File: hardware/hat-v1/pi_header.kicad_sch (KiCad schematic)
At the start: 12 parts, among them J2 Pi 40-pin (female, 11 mm stac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, U10 CAT24C32WI-GT3

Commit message: HAT v1 schematic: apply adversarial review (power + digital/security/DFM)
AUTO-ON above buck EN window, BENCH no longer blocks power-off, OVP moved
to 19.2 V with input damper, Tier A parts DNP for JLC, debug links
removable for production, antenna short limited, stock footprints where
available, cap ratings/DC-bias fixes, CONSOLE_TX/RX naming.

Co-Authored-By: Claude Opus 5.5 <noreply@anthropic.com>
Claude-Session: https://claude.ai/code/session_01MLRuxTEmuMV82xcNLE62jW
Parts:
- H1, H2, H3, H4, JP4: now left out of the parts list
- U10: now not fitted
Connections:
- net UART0_RX renamed CONSOLE_RX
- net UART0_TX renamed CONSOLE_TX
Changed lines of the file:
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@@
     (property "Intersheetrefs" "${INTERSHEET_REFS}" (at 81.28 33.02 0) (effects (font (size 1.27 1.27)) hide)))
   (wire (pts (xy 78.74 35.56) (xy 81.28 35.56)) (stroke (width 0) (type default)))
-  (global_label "UART0_TX" (shape passive) (at 81.28 35.56 0) (fields_autoplaced) (effects (font (size 1.27 1.27)) (justify left))
+  (global_label "CONSOLE_TX" (shape passive) (at 81.28 35.56 0) (fields_autoplaced) (effects (font (size 1.27 1.27)) (justify left))
     (property "Intersheetrefs" "${INTERSHEET_REFS}" (at 81.28 35.56 0) (effects (font (size 1.27 1.27)) hide)))
   (wire (pts (xy 78.74 38.1) (xy 81.28 38.1)) (stroke (width 0) (type default)))
-  (global_label "UART0_RX" (shape passive) (at 81.28 38.1 0) (fields_autoplaced) (effects (font (size 1.27 1.27)) (justify left))
+  (global_label "CONSOLE_RX" (shape passive) (at 81.28 38.1 0) (fields_autoplaced) (effects (font (size 1.27 1.27)) (justify left))
     (property "Intersheetrefs" "${INTERSHEET_REFS}" (at 81.28 38.1 0) (effects (font (size 1.27 1.27)) hide)))
   (wire (pts (xy 78.74 40.64) (xy 81.28 40.64)) (stroke (width 0) (type default)))
@@
   (global_label "SPI1_SCLK" (shape passive) (at 81.28 76.2 0) (fields_autoplaced) (effects (font (size 1.27 1.27)) (justify left))
     (property "Intersheetrefs" "${INTERSHEET_REFS}" (at 81.28 76.2 0) (effects (font (size 1.27 1.27)) hide)))
-  (symbol (lib_id "batman:EEPROM_24") (at 121.92 34.29 0) (unit 1) (in_bom yes) (on_board yes) (dnp no)
+  (symbol (lib_id "batman:EEPROM_24") (at 121.92 34.29 0) (unit 1) (in_bom yes) (on_board yes) (dnp yes)
     (property "Reference" "U10" (at 115.57 24.13 0) (effects (font (size 1.27 1.27)) (justify left bottom)))
     (property "Value" "CAT24C32WI-GT3" (at 115.57 45.72 0) (effects (font (size 1.27 1.27)) (justify left top)))
@@
   (global_label "3V3_PI" (shape passive) (at 200.66 26.67 0) (fields_autoplaced) (effects (font (size 1.27 1.27)) (justify left))
     (property "Intersheetrefs" "${INTERSHEET_REFS}" (at 200.66 26.67 0) (effects (font (size 1.27 1.27)) hide)))
-  (symbol (lib_id "batman:SJ") (at 228.6 26.67 0) (unit 1) (in_bom yes) (on_board yes) (dnp no)
+  (symbol (lib_id "batman:SJ") (at 228.6 26.67 0) (unit 1) (in_bom no) (on_board yes) (dnp no)
     (property "Reference" "JP4" (at 228.6 24.13 0) (effects (font (size 1.27 1.27)) (justify bottom)))
     (property "Value" "EEP-WRITE (open)" (at 228.6 29.21 0) (effects (font (size 1.27 1.27)) (justify top)))
@@
   (global_label "3V3_PI" (shape passive) (at 115.57 90.17 0) (fields_autoplaced) (effects (font (size 1.27 1.27)) (justify left))
     (property "Intersheetrefs" "${INTERSHEET_REFS}" (at 115.57 90.17 0) (effects (font (size 1.27 1.27)) hide)))
-  (symbol (lib_id "batman:MH") (at 142.24 90.17 0) (unit 1) (in_bom yes) (on_board yes) (dnp no)
+  (symbol (lib_id "batman:MH") (at 142.24 90.17 0) (unit 1) (in_bom no) (on_board yes) (dnp no)
     (property "Reference" "H1" (at 142.24 87.63 0) (effects (font (size 1.27 1.27)) (justify bottom)))
     (property "Value" "M2.5" (at 142.24 92.71 0) (effects (font (size 1.27 1.27)) (justify top)))
@@
   (global_label "GND" (shape passive) (at 137.16 90.17 180) (fields_autoplaced) (effects (font (size 1.27 1.27)) (justify right))
     (property "Intersheetrefs" "${INTERSHEET_REFS}" (at 137.16 90.17 0) (effects (font (size 1.27 1.27)) hide)))
-  (symbol (lib_id "batman:MH") (at 162.56 90.17 0) (unit 1) (in_bom yes) (on_board yes) (dnp no)
+  (symbol (lib_id "batman:MH") (at 162.56 90.17 0) (unit 1) (in_bom no) (on_board yes) (dnp no)
     (property "Reference" "H2" (at 162.56 87.63 0) (effects (font (size 1.27 1.27)) (justify bottom)))
     (property "Value" "M2.5" (at 162.56 92.71 0) (effects (font (size 1.27 1.27)) (justify top)))
@@
   (global_label "GND" (shape passive) (at 157.48 90.17 180) (fields_autoplaced) (effects (font (size 1.27 1.27)) (justify right))
     (property "Intersheetrefs" "${INTERSHEET_REFS}" (at 157.48 90.17 0) (effects (font (size 1.27 1.27)) hide)))
-  (symbol (lib_id "batman:MH") (at 182.88 90.17 0) (unit 1) (in_bom yes) (on_board yes) (dnp no)
+  (symbol (lib_id "batman:MH") (at 182.88 90.17 0) (unit 1) (in_bom no) (on_board yes) (dnp no)
     (property "Reference" "H3" (at 182.88 87.63 0) (effects (font (size 1.27 1.27)) (justify bottom)))
     (property "Value" "M2.5" (at 182.88 92.71 0) (effects (font (size 1.27 1.27)) (justify top)))
@@
   (global_label "GND" (shape passive) (at 177.8 90.17 180) (fields_autoplaced) (effects (font (size 1.27 1.27)) (justify right))
     (property "Intersheetrefs" "${INTERSHEET_REFS}" (at 177.8 90.17 0) (effects (font (size 1.27 1.27)) hide)))
-  (symbol (lib_id "batman:MH") (at 203.2 90.17 0) (unit 1) (in_bom yes) (on_board yes) (dnp no)
+  (symbol (lib_id "batman:MH") (at 203.2 90.17 0) (unit 1) (in_bom no) (on_board yes) (dnp no)
     (property "Reference" "H4" (at 203.2 87.63 0) (effects (font (size 1.27 1.27)) (justify bottom)))
     (property "Value" "M2.5" (at 203.2 92.71 0) (effects (font (size 1.27 1.27)) (justify top)))

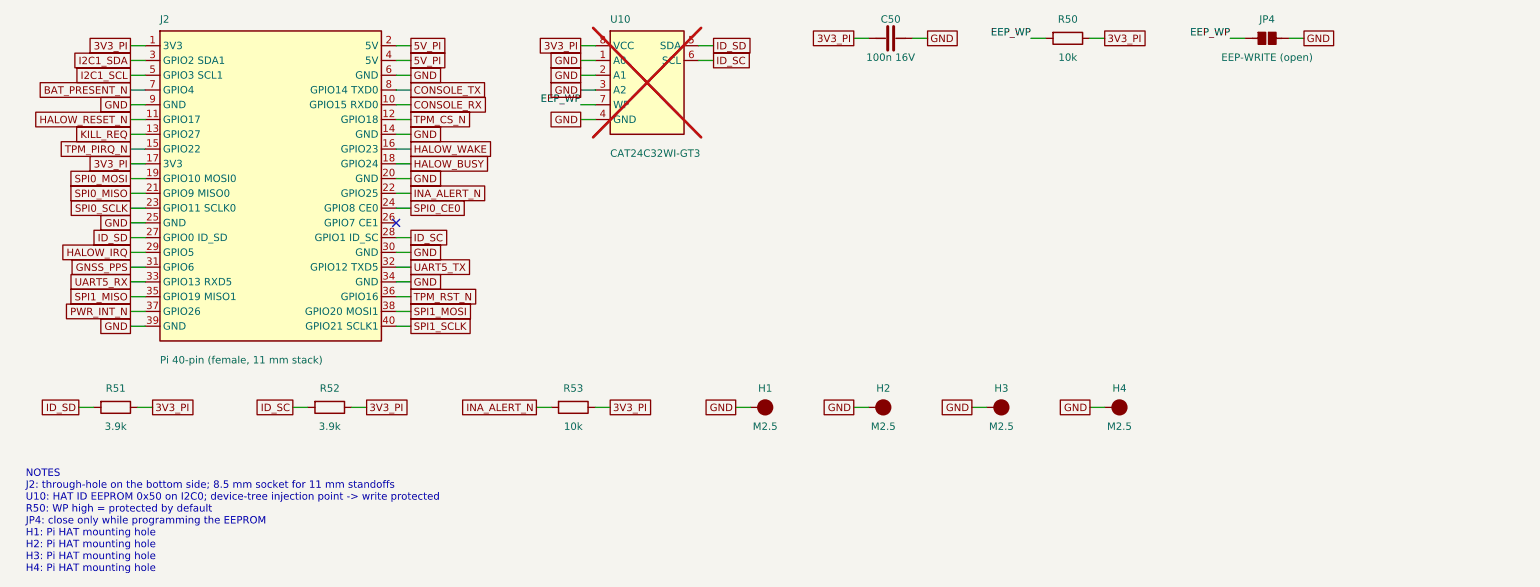
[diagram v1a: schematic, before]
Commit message: HAT v1: reduce test points (clip pads only for VBAT/5V/3V3 HaLow/GND), re-place
Signals on the 40-pin header are probed on its solder joints; checker
verifies that list. Floorplan: all functional parts and the 4 clip pads
fit; 23 small probe pads still need a home.

Co-Authored-By: Claude Opus 5.5 <noreply@anthropic.com>
Claude-Session: https://claude.ai/code/session_01MLRuxTEmuMV82xcNLE62jW
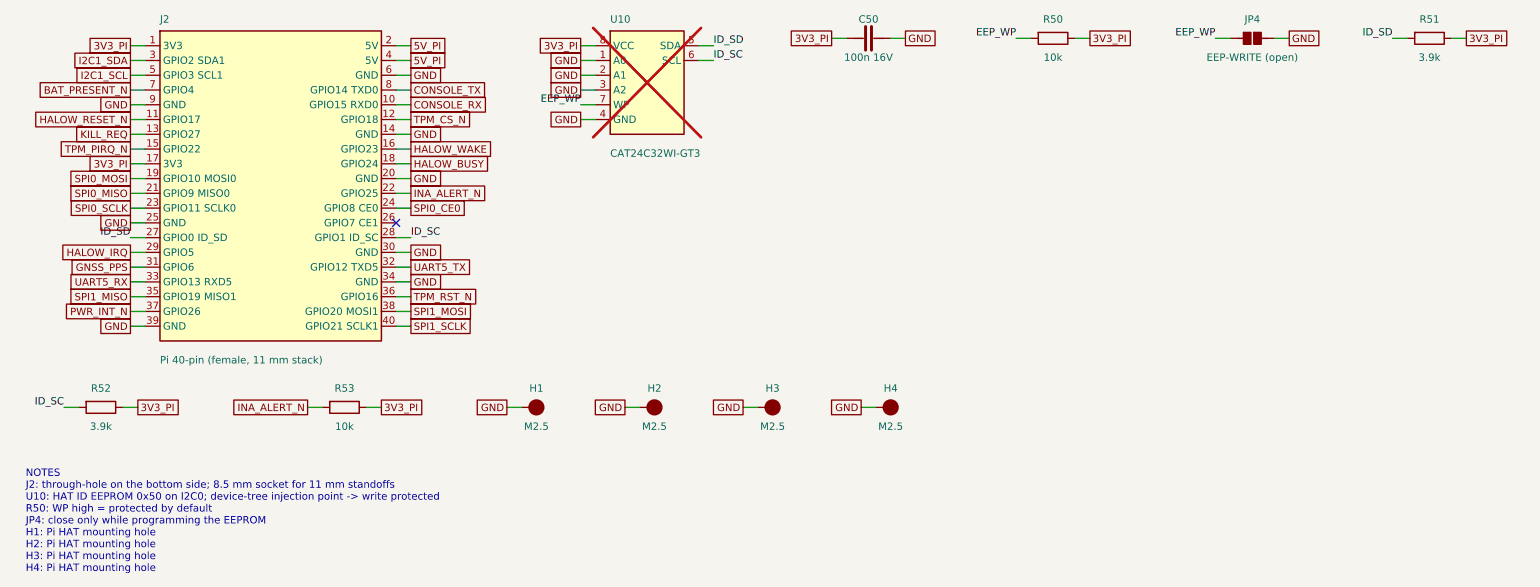
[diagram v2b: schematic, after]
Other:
- moved on the sheet: C50, H1, H2, H3, H4, JP4, R50, R51, R52, R53

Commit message: HAT v1: option D power tree - HaLow 3.3 V buck fed from the Pi 5 V rail
- TPS62933F input moved from the OR node to 5V_PI (HAT 5 V buck or Pi USB-C),
  as on the WM1302 HAT: the HaLow card still runs on USB-C only
- EN pulled up to the Pi 3.3 V through 100k: no back-feed into an unpowered Pi,
  HAT+ STANDBY turns the card off; LTC2955 off already removes 5 V
- removed: LM74700 x2 + FET x2 + VCAP x2 (OR-ing), BENCH jumper + Q9/R24, Q8,
  HAT ID EEPROM + WP jumper + pull-ups + decoupling, OR_NODE test point
- kept the battery-present divider (spec review #22)
- checker: HaLow EN set points; spec 5.5.5 power tree review; re-placed board

Co-Authored-By: Claude Opus 5.5 <noreply@anthropic.com>
Claude-Session: https://claude.ai/code/session_01MLRuxTEmuMV82xcNLE62jW
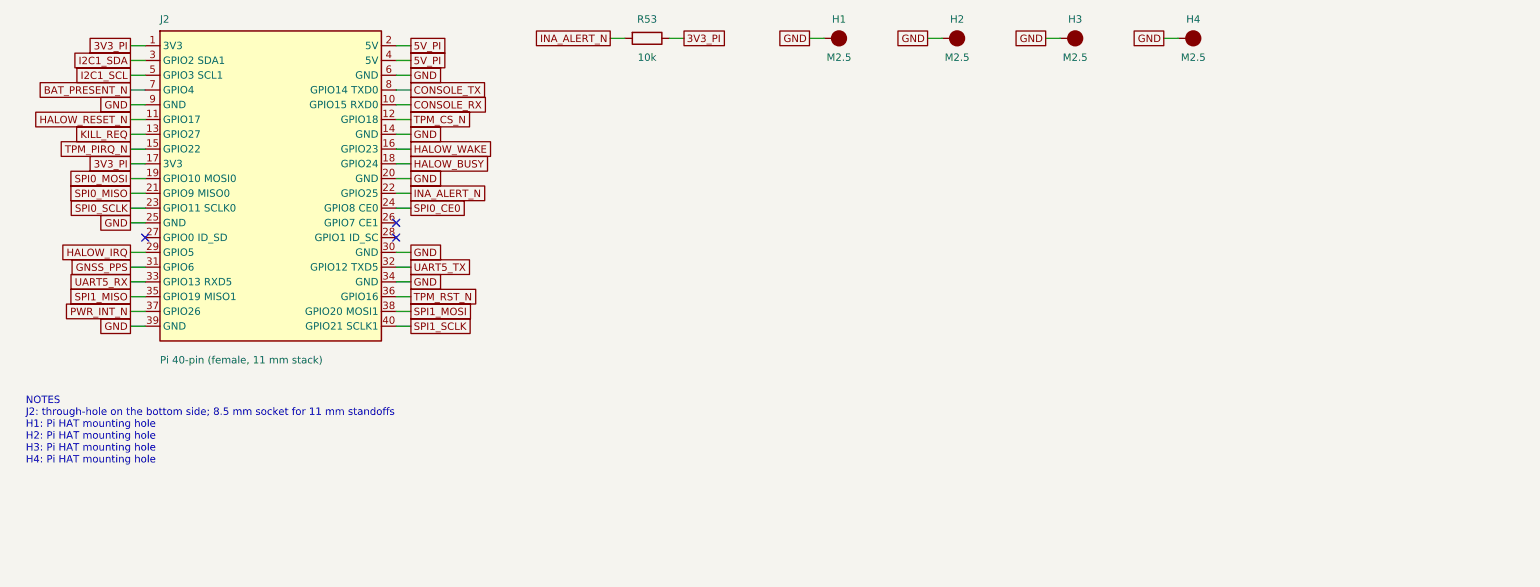
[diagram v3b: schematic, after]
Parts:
- removed C50: 100n 16V, Capacitor_SMD:C_0402_1005Metric, symbol batman:C
- removed JP4: EEP-WRITE (open), Jumper:SolderJumper-2_P1.3mm_Open_RoundedPad1.0x1.5mm, symbol batman:SJ
- removed R50: 10k, Resistor_SMD:R_0402_1005Metric, symbol batman:R
- removed R51, R52: 3.9k, Resistor_SMD:R_0402_1005Metric, symbol batman:R
- removed U10: CAT24C32WI-GT3, Package_SO:SOIC-8_3.9x4.9mm_P1.27mm, symbol batman:EEPROM_24
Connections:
- net ID_SC: no longer names the net of J2.28 (GPIO1 ID_SC)
- net ID_SD: no longer names the net of J2.27 (GPIO0 ID_SD)
- no-connect marks 1 -> 3
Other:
- note added: "NOTES J2: through-hole on the bottom side; 8.5 mm socket for 11 mm standoffs H1: Pi HAT mounting hole H2: Pi HAT mounting hole H3: Pi HAT mounting hole H4: Pi HAT mounting hole"
- note removed: "NOTES J2: through-hole on the bottom side; 8.5 mm socket for 11 mm standoffs U10: HAT ID EEPROM 0x50 on I2C0; device-tree injection point -> write protected R50: WP high = protected by default JP4: close only while programming the EEPROM H1: Pi HAT mounting hole H2: Pi HAT mounting hole H3: Pi HAT mounting hole H4: Pi HAT mounting hole"
- moved on the sheet: H1, H2, H3, H4, R53

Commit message: HAT v1: looser placement for routability
- packer keeps a routing ring around each part: 1.0 mm for ICs / FETs / connectors,
  0.5 mm for passives (was 0.2 mm for everything)
- eFuse column moved in from the left edge; 0.45 mm track/via keep-out ring at the board edge
- H1 is a plain NPTH hole (it sits in the Pi 4 Wi-Fi keep-out)
- power-track widening now clears tracks it already widened, and skips the Wi-Fi keep-outs
- min drill 0.2 mm (QFN thermal vias); probe pads stay off IC pads that reach B.Cu

Co-Authored-By: Claude Opus 5.5 <noreply@anthropic.com>
Claude-Session: https://claude.ai/code/session_01MLRuxTEmuMV82xcNLE62jW
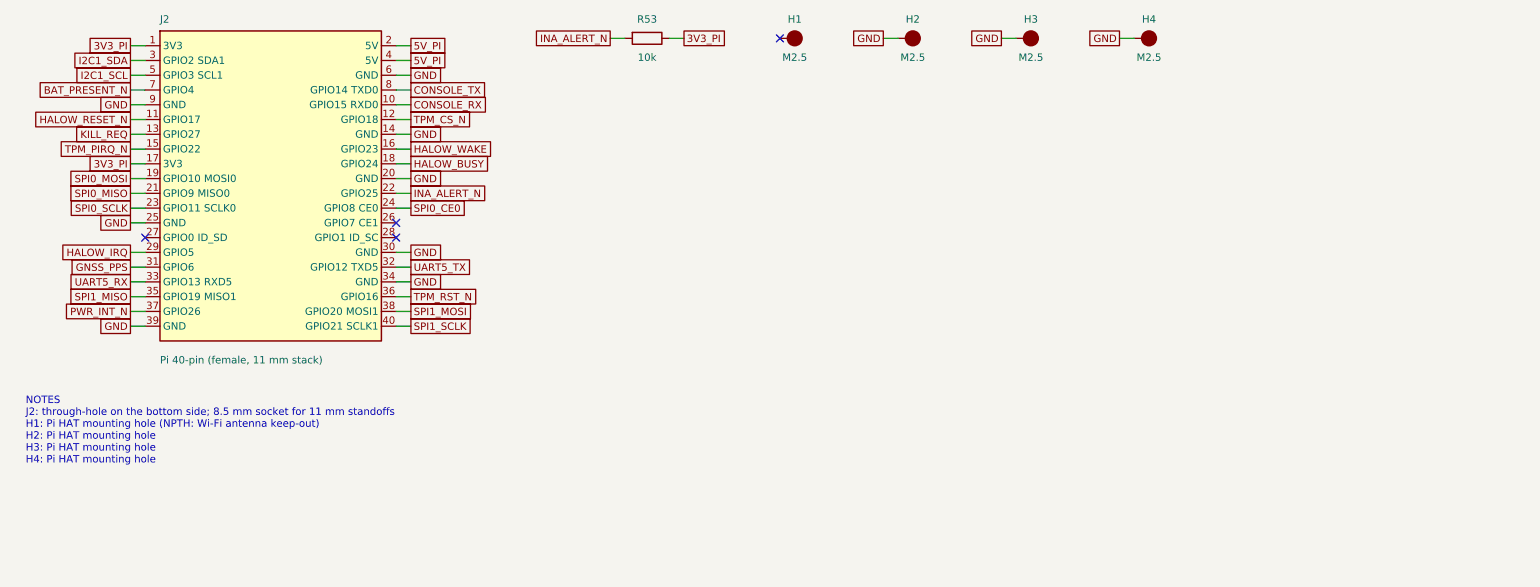
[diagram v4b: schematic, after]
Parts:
- H1: footprint MountingHole:MountingHole_2.7mm_M2.5_Pad_Via -> MountingHole:MountingHole_2.7mm_M2.5; Note Pi HAT mounting hole -> Pi HAT mounting hole (NPTH: Wi-Fi antenna keep-out)
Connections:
- net GND: no longer H1.1
- no-connect marks 3 -> 4
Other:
- note added: "NOTES J2: through-hole on the bottom side; 8.5 mm socket for 11 mm standoffs H1: Pi HAT mounting hole (NPTH: Wi-Fi antenna keep-out) H2: Pi HAT mounting hole H3: Pi HAT mounting hole H4: Pi HAT mounting hole"
- note removed: "NOTES J2: through-hole on the bottom side; 8.5 mm socket for 11 mm standoffs H1: Pi HAT mounting hole H2: Pi HAT mounting hole H3: Pi HAT mounting hole H4: Pi HAT mounting hole"
- moved on the sheet: H1, H2, H3, H4
